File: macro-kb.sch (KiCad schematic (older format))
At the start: 27 parts

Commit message: board
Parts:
- removed C? (x2): 22pF, symbol Device:C_Small
- removed Y?: 16MHz, symbol Device:Crystal_GND2_Small
- added C10, C11, C12, C13, C14, C15, C16, C7, C8, C9: 0.1uF, Capacitor_SMD:C_0603_1608Metric, symbol Device:C_Small
- added C17: 100uF, Capacitor_SMD:C_1210_3225Metric, symbol Device:C_Small
- added C5, C6: 22pF, Capacitor_SMD:C_0603_1608Metric, symbol Device:C_Small
- added D10, D7, D8, D9: WS2812B, LED_SMD:LED_WS2812B_PLCC4_5.0x5.0mm_P3.2mm, symbol LED:WS2812B
- added D11, D12, D13, D14, D15, D16: SK6805, LED_SMD:LED_SK6805_PLCC4_2.4x2.7mm_P1.3mm, symbol LED:SK6805
- added Y1: 16MHz 18pF, Crystal:Crystal_SMD_3225-4Pin_3.2x2.5mm, symbol Device:Crystal_GND2_Small
- C1, C4: renamed from C?; footprint (none) -> Capacitor_SMD:C_0603_1608Metric
- C2, C3: renamed from C?; footprint (none) -> Capacitor_SMD:C_0402_1005Metric
- D1, D2, D3, D4, D5, D6: renamed from D?; footprint (none) -> Diode_SMD:D_SOD-123
- F1: renamed from F?; footprint (none) -> Fuse:Fuse_0805_2012Metric
- MX1, MX2, MX3, MX4, MX5, MX6: renamed from MX?; footprint (none) -> Button_Switch_Keyboard:SW_Cherry_MX_1.00u_PCB
- R1, R2, R3, R4: renamed from R?; footprint (none) -> Resistor_SMD:R_0603_1608Metric
- SW1: renamed from SW?; footprint (none) -> Button_Switch_SMD:Panasonic_EVQPUL_EVQPUC
- USB1: renamed from USB?; value Molex-0548190589 -> Mini B; footprint (none) -> Connector_USB:USB_Mini-B_Lumberg_2486_01_Horizontal; symbol random-keyboard-parts:Molex-0548190589 -> Connector:USB_B_Mini
- gave numbers to parts that had none: 1
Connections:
- net +5V: now also C10.1, C11.1, C12.1, C13.1, C14.1, C15.1, C16.1, C17.2, C7.1, C8.1, C9.1, D10.1 (VDD), D11.4 (VDD), D12.4 (VDD), D13.4 (VDD), D14.4 (VDD), D15.4 (VDD), D16.4 (VDD), D7.1 (VDD), D8.1 (VDD), D9.1 (VDD)
- net COL0: now also U1.14 (PB0)
- net COL1: now also U1.15 (PB1)
- net COL2: now also U1.16 (PB2)
- net D+: now also USB1.2 (D-); no longer USB1.3 (D+)
- net D-: now also USB1.3 (D+); no longer USB1.4 (D-)
- net GND: now also USB1.5 (GND), C10.2, C11.2, C12.2, C13.2, C14.2, C15.2, C16.2, C17.1, C5.2, C6.2, C7.2, C8.2, C9.2, D10.3 (VSS), D11.2 (VSS), D12.2 (VSS), D13.2 (VSS), D14.2 (VSS), D15.2 (VSS), D16.2 (VSS), D7.3 (VSS), D8.3 (VSS), D9.3 (VSS), Y1.2; no longer USB1.1 (GND)
- net ROW0: now also U1.17 (PB3)
- net ROW1: now also U1.18 (PB4)
- net VCC: now also USB1.1 (VBUS); no longer USB1.5 (VBUS)
- net at U1.1 (XTAL1): now also C5.1, Y1.1
- net ROW2: now reaches U1.19 (PB5)
- net at U1.2 (PC0/XTAL2): now also C6.1, Y1.3
- net KEY_LEDS: now reaches U1.8 (PD2)
- net KEY_LEDS: now also D11.3 (DIN)
- net UNDERGLOW_LEDS: now reaches U1.9 (PD3)
- net UNDERGLOW_LEDS: now also D7.4 (DIN)
- new net: D11.1 (DOUT), D12.3 (DIN)
- new net: D12.1 (DOUT), D13.3 (DIN)
- new net: D13.1 (DOUT), D14.3 (DIN)
- new net: D14.1 (DOUT), D15.3 (DIN)
- new net: D15.1 (DOUT), D16.3 (DIN)
- new net: D7.2 (DOUT), D8.4 (DIN)
- new net: D8.2 (DOUT), D9.4 (DIN)
- new net: D10.4 (DIN), D9.2 (DOUT)
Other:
- moved on the sheet: C1, C2, C3, C4, D1, D2, D3, D4, D5, D6, F1, MX1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

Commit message: routed
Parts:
- F1: value Polyfuse -> 500mA
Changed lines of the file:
@@
 P 2900 4700
 F 0 "F1" V 2675 4700 50  0000 C CNN
-F 1 "Polyfuse" V 2766 4700 50  0000 C CNN
+F 1 "500mA" V 2766 4700 50  0000 C CNN
 F 2 "Fuse:Fuse_0805_2012Metric" H 2950 4500 50  0001 L CNN
 F 3 "~" H 2900 4700 50  0001 C CNN

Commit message: final version (hopefully)
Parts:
- added R5: 470, Resistor_SMD:R_0603_1608Metric, symbol Device:R_Small
- D1, D2, D3, D4, D5, D6: value SOD-123 -> SOD-123F; footprint Diode_SMD:D_SOD-123 -> Diode_SMD:D_SOD-123F
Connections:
- net KEY_LEDS: now also R5.2; no longer D11.3 (DIN)
- net UNDERGLOW_LEDS: now also D16.1 (DOUT); no longer U1.9 (PD3)
- net ROW2: no longer names the net of U1.19 (PB5)
- new net: D11.3 (DIN), R5.1
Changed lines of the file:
@@
 P 2200 6600
 F 0 "D1" H 2200 6700 50  0000 R CNN
-F 1 "SOD-123" H 2575 6700 50  0000 R CNN
-F 2 "Diode_SMD:D_SOD-123" V 2200 6600 50  0001 C CNN
+F 1 "SOD-123F" H 2575 6700 50  0000 R CNN
+F 2 "Diode_SMD:D_SOD-123F" V 2200 6600 50  0001 C CNN
 F 3 "~" V 2200 6600 50  0001 C CNN
 	1    2200 6600
@@
 P 2875 6600
 F 0 "D2" H 2875 6700 50  0000 R CNN
-F 1 "SOD-123" H 3250 6700 50  0000 R CNN
-F 2 "Diode_SMD:D_SOD-123" V 2875 6600 50  0001 C CNN
+F 1 "SOD-123F" H 3250 6700 50  0000 R CNN
+F 2 "Diode_SMD:D_SOD-123F" V 2875 6600 50  0001 C CNN
 F 3 "~" V 2875 6600 50  0001 C CNN
 	1    2875 6600
@@
 	1    0    0    -1
 $EndComp
-$Comp
-L Device:D_Small D3
-U 1 1 5CF0182A
-P 3550 6600
-F 0 "D3" H 3550 6700 50  0000 R CNN
-F 1 "SOD-123" H 3925 6700 50  0000 R CNN
-F 2 "Diode_SMD:D_SOD-123" V 3550 6600 50  0001 C CNN
-F 3 "~" V 3550 6600 50  0001 C CNN
-	1    3550 6600
-	0    -1   -1   0
-$EndComp
 Wire Wire Line
 	3675 6475 3550 6475
@@
 P 2200 7350
 F 0 "D4" H 2200 7450 50  0000 R CNN
-F 1 "SOD-123" H 2575 7450 50  0000 R CNN
-F 2 "Diode_SMD:D_SOD-123" V 2200 7350 50  0001 C CNN
+F 1 "SOD-123F" H 2575 7450 50  0000 R CNN
+F 2 "Diode_SMD:D_SOD-123F" V 2200 7350 50  0001 C CNN
 F 3 "~" V 2200 7350 50  0001 C CNN
 	1    2200 7350
@@
 P 2875 7350
 F 0 "D5" H 2875 7450 50  0000 R CNN
-F 1 "SOD-123" H 3250 7450 50  0000 R CNN
-F 2 "Diode_SMD:D_SOD-123" V 2875 7350 50  0001 C CNN
+F 1 "SOD-123F" H 3250 7450 50  0000 R CNN
+F 2 "Diode_SMD:D_SOD-123F" V 2875 7350 50  0001 C CNN
 F 3 "~" V 2875 7350 50  0001 C CNN
 	1    2875 7350
@@
 P 3550 7350
 F 0 "D6" H 3550 7450 50  0000 R CNN
-F 1 "SOD-123" H 3925 7450 50  0000 R CNN
-F 2 "Diode_SMD:D_SOD-123" V 3550 7350 50  0001 C CNN
+F 1 "SOD-123F" H 3925 7450 50  0000 R CNN
+F 2 "Diode_SMD:D_SOD-123F" V 3550 7350 50  0001 C CNN
 F 3 "~" V 3550 7350 50  0001 C CNN
 	1    3550 7350
@@
 $EndComp
 Connection ~ 6150 5800
-Text GLabel 5650 4500 0    50   Input ~ 0
+Text GLabel 5300 4500 0    50   Input ~ 0
 KEY_LEDS
-Wire Wire Line
-	5650 4500 5850 4500
 $Comp
 L power:+5V #PWR0109
@@
 Wire Wire Line
 	8650 1600 9100 1600
-Text GLabel 5650 1600 0    50   Input ~ 0
+Text GLabel 5600 1600 0    50   Input ~ 0
 UNDERGLOW_LEDS
-Wire Wire Line
-	5650 1600 5950 1600
 $Comp
 L Device:C_Small C7
@@
 Text GLabel 3750 1700 2    50   Input ~ 0
 ROW1
-Text GLabel 3750 1800 2    50   Input ~ 0
-ROW2
 Text GLabel 3750 3000 2    50   Input ~ 0
 KEY_LEDS
-Text GLabel 3750 3100 2    50   Input ~ 0
+Text GLabel 8650 5800 2    50   Input ~ 0
 UNDERGLOW_LEDS
 Wire Wire Line
@@
 	3750 1700 3550 1700
 Wire Wire Line
-	3750 1800 3550 1800
-Wire Wire Line
 	3750 3000 3550 3000
 Wire Wire Line
-	3750 3100 3550 3100
+	8650 5800 8450 5800
+$Comp
+L Device:D_Small D3
+U 1 1 5CF0182A
+P 3550 6600
+F 0 "D3" H 3550 6700 50  0000 R CNN
+F 1 "SOD-123F" H 3925 6700 50  0000 R CNN
+F 2 "Diode_SMD:D_SOD-123F" V 3550 6600 50  0001 C CNN
+F 3 "~" V 3550 6600 50  0001 C CNN
+	1    3550 6600
+	0    -1   -1   0
+$EndComp
+$Comp
+L Device:R_Small R5
+U 1 1 5CF1CB9F
+P 5550 4500
+F 0 "R5" V 5354 4500 50  0000 C CNN
+F 1 "470" V 5445 4500 50  0000 C CNN
+F 2 "Resistor_SMD:R_0603_1608Metric" H 5550 4500 50  0001 C CNN
+F 3 "~" H 5550 4500 50  0001 C CNN
+	1    5550 4500
+	0    1    1    0
+$EndComp
+Wire Wire Line
+	5850 4500 5650 4500
+Wire Wire Line
+	5450 4500 5300 4500
+Wire Wire Line
+	8450 5500 8450 5800
+Wire Wire Line
+	5600 1600 5950 1600
 $EndSCHEMATC

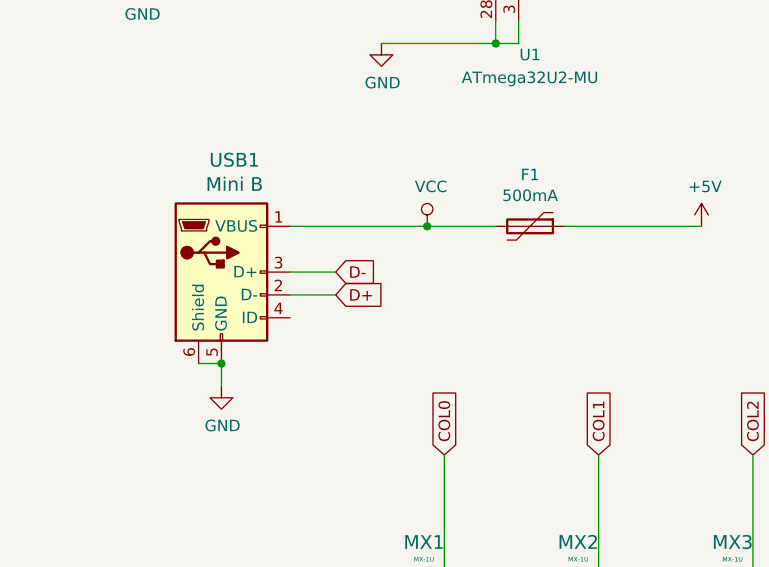
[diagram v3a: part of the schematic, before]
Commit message: fixed crossed USB lines v1.1
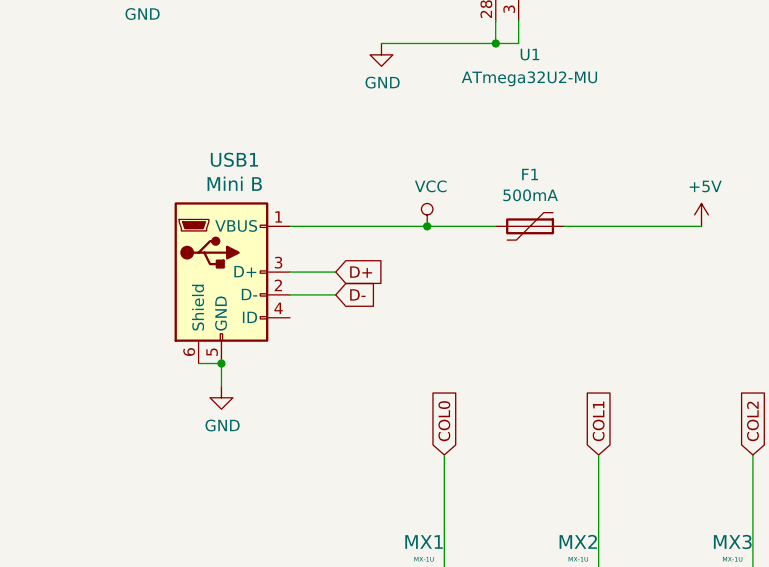
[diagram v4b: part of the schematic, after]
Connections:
- net D+: now also USB1.3 (D+); no longer USB1.2 (D-)
- net D-: now also USB1.2 (D-); no longer USB1.3 (D+)
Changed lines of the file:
@@
 Wire Wire Line
 	2450 4700 2750 4700
+Text GLabel 2050 4900 2    50   Input ~ 0
+D+
 Text GLabel 2050 5000 2    50   Input ~ 0
-D+
-Text GLabel 2050 4900 2    50   Input ~ 0
 D-
 Wire Wire Line
 	1850 4700 2450 4700
 Connection ~ 2450 4700
-Wire Wire Line
-	1850 4900 2050 4900
-Wire Wire Line
-	1850 5000 2050 5000
 $Comp
 L power:GND #PWR013
@@
 Wire Wire Line
 	5600 1600 5950 1600
+Wire Wire Line
+	1850 4900 2050 4900
+Wire Wire Line
+	1850 5000 2050 5000
 $EndSCHEMATC
